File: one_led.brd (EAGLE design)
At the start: 3 parts, among them U1_ WS2812B_LED

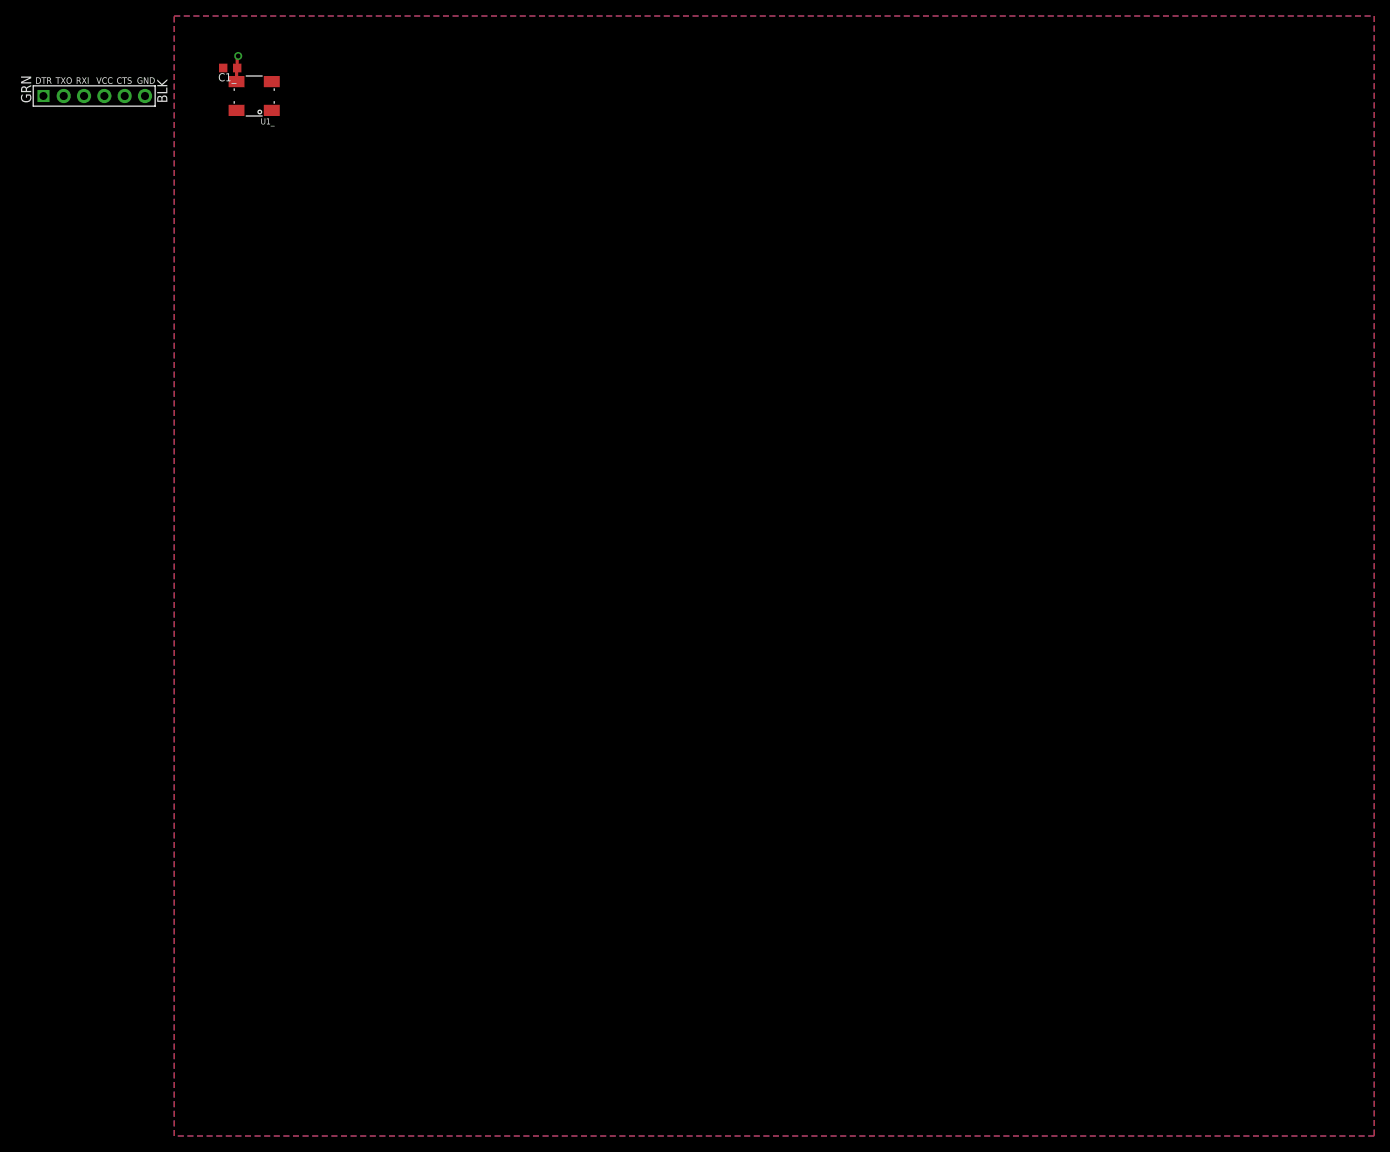
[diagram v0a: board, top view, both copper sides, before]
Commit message: Bugfix: Automatically connect array inputs and outputs to any non-array parts that reference them.
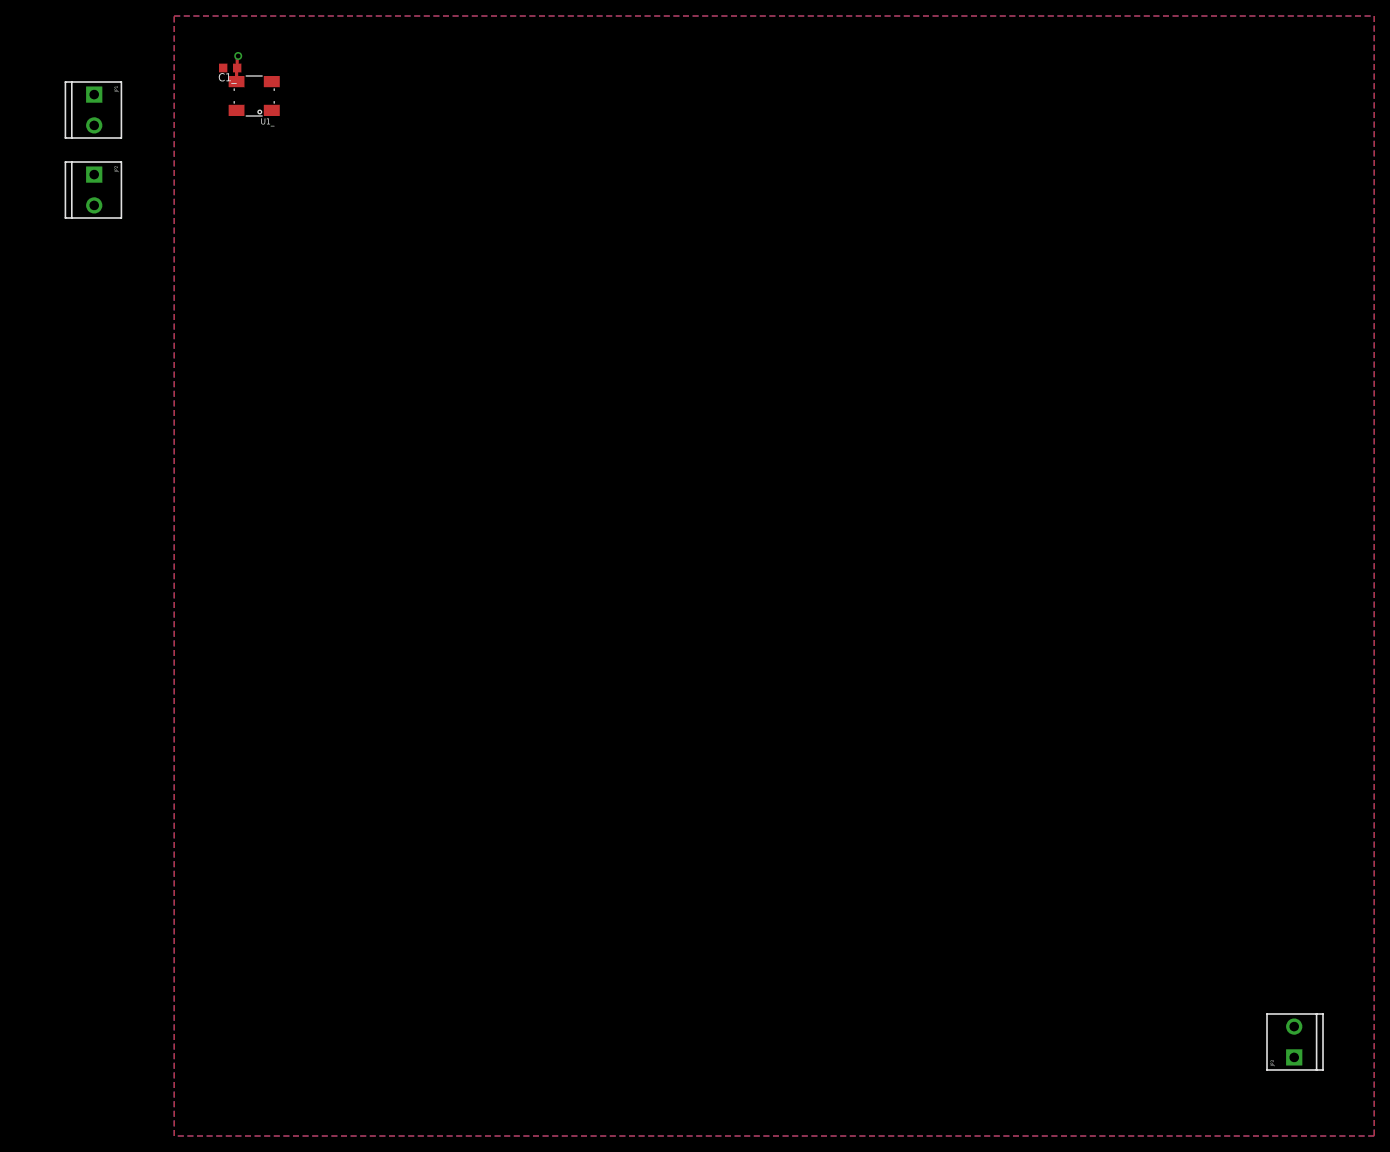
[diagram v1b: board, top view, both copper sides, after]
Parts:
- added JP2: POWER, SparkFun-Connectors:SCREWTERMINAL-3.5MM-2_LOCK
- added JP3: DATA_IN, SparkFun-Connectors:SCREWTERMINAL-3.5MM-2_LOCK
- JP1: value FTDI_DEVICE -> DATA_IN; device SparkFun-Connectors:FTDI_DEVICE_SIDE -> SparkFun-Connectors:SCREWTERMINAL-3.5MM-2_LOCK
- turned JP1 to 270 degrees
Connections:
- new net 1IN: JP1.2
- new net 1OUT: JP3.2
- net 5V: now also JP2.2
- net GND: now also JP1.1, JP2.1, JP3.1
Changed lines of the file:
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@@
 <element name="U1_" library="blinkinlabs" package="WS2812B_LED" value="WS2812B_LED" x="0" y="0" rot="R180"/>
 <element name="C1_" library="adafruit" package="C0603K" value="" x="-3" y="3.5" rot="R180"/>
-<element name="JP1" library="SparkFun-Connectors" package="FTDI_DEVICE_SIDE" value="FTDI_DEVICE" x="-20" y="0"/>
+<element name="JP1" library="SparkFun-Connectors" package="SCREWTERMINAL-3.5MM-2_LOCK" value="DATA_IN" x="-20" y="0" rot="R270"/>
+<element name="JP2" library="SparkFun-Connectors" package="SCREWTERMINAL-3.5MM-2_LOCK" value="POWER" x="-20" y="-10" rot="R270"/>
+<element name="JP3" library="SparkFun-Connectors" package="SCREWTERMINAL-3.5MM-2_LOCK" value="DATA_IN" x="130" y="-120" rot="R90"/>
 </elements>
 <signals>
@@
 <wire x1="-2.125" y1="3.5" x2="-2.125" y2="4.875" width="0.4064" layer="1"/>
 <wire x1="-2.125" y1="4.875" x2="-2" y2="5" width="0.4064" layer="1"/>
+<contactref element="JP2" pad="2"/>
+<wire x1="-2.2" y1="1.8" x2="-20" y2="-13.6778" width="0" layer="19" extent="1-1"/>
 </signal>
 <signal name="GND">
@@
 <vertex x="-10" y="-130"/>
 </polygon>
+<contactref element="JP1" pad="1"/>
+<contactref element="JP2" pad="1"/>
+<contactref element="JP3" pad="1"/>
+<wire x1="-20" y1="-9.8222" x2="130" y2="-120.1778" width="0" layer="19" extent="1-1"/>
+<wire x1="-20" y1="0.1778" x2="-20" y2="-9.8222" width="0" layer="19" extent="1-1"/>
+<wire x1="-3.875" y1="3.5" x2="-20" y2="0.1778" width="0" layer="19" extent="1-1"/>
+<wire x1="2.2" y1="-1.8" x2="-3.875" y2="3.5" width="0" layer="19" extent="1-1"/>
+</signal>
+<signal name="1IN">
+<contactref element="JP1" pad="2"/>
+</signal>
+<signal name="1OUT">
+<contactref element="JP3" pad="2"/>
 </signal>
 </signals>
